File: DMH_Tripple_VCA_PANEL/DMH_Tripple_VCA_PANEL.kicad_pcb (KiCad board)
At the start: 2 copper layers, 50 x 200 mm, 21 parts, among them J0 Panel_GND_Solder_Wire_Pad

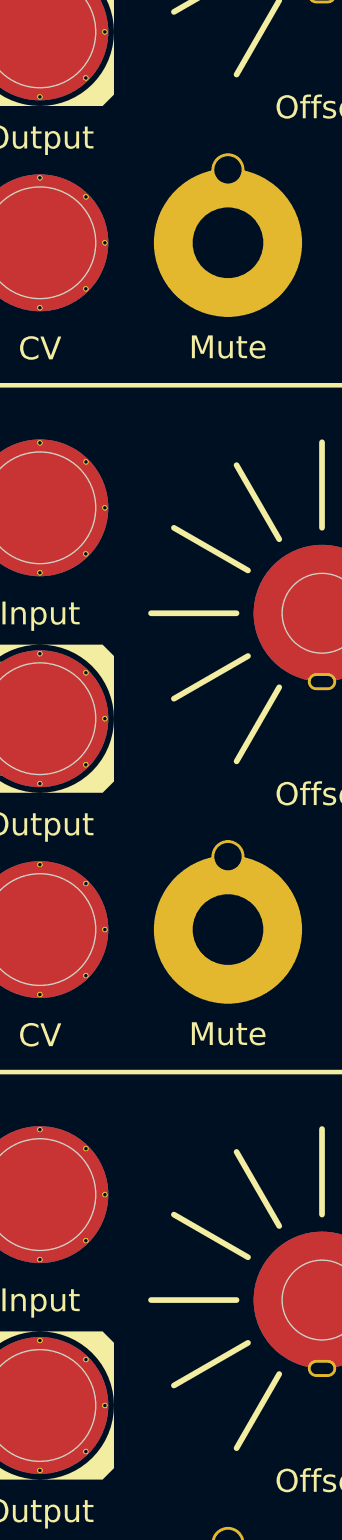
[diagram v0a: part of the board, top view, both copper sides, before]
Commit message: Added LED holes
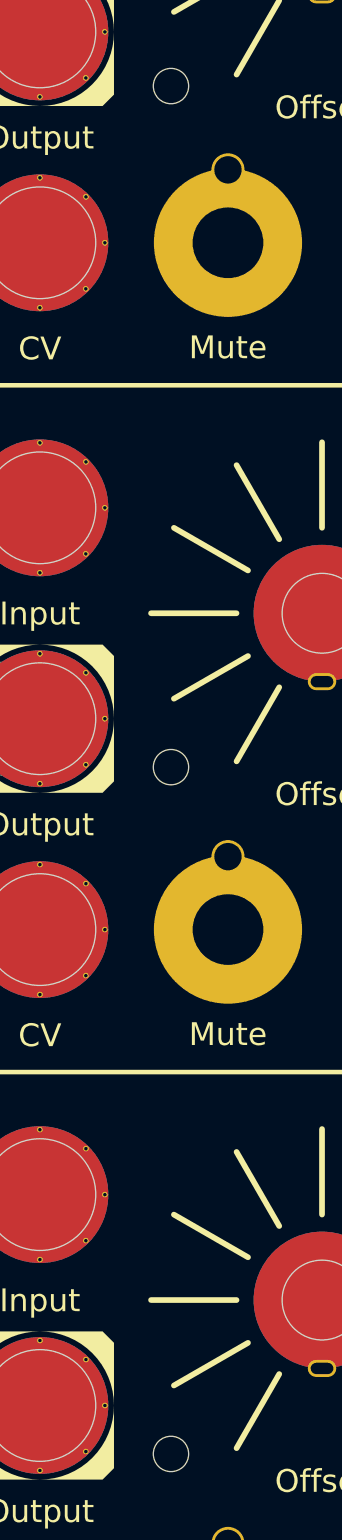
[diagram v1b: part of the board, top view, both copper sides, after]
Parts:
- added H17: LED, SynthStuff:MountingHole_LED_3mm, F.Cu at (70.0, 74.5)
- added H22: LED, SynthStuff:MountingHole_LED_3mm, F.Cu at (70.0, 134.2)
- added H23: LED, SynthStuff:MountingHole_LED_3mm, F.Cu at (70.0, 194.5)

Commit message: Finished Schematic
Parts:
- H17, H22, H23: footprint SynthStuff:MountingHole_LED_3mm -> SynthStuff:MountingHole_LED_5mm
- H18: value Mix Out + -> Mix Out
- moved J0 40.0 mm to (95.0, 130.0)

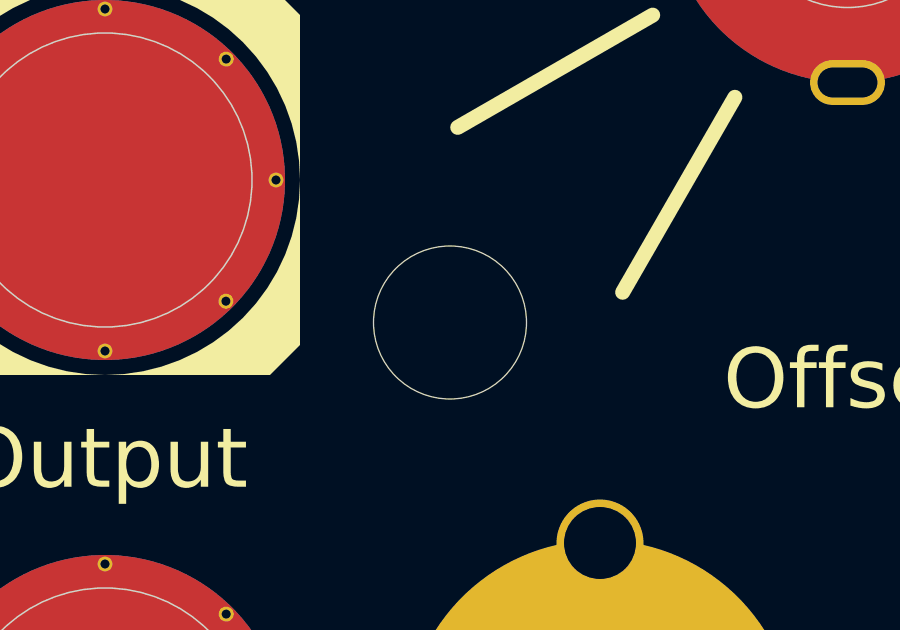
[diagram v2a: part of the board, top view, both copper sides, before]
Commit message: Fixed LED position
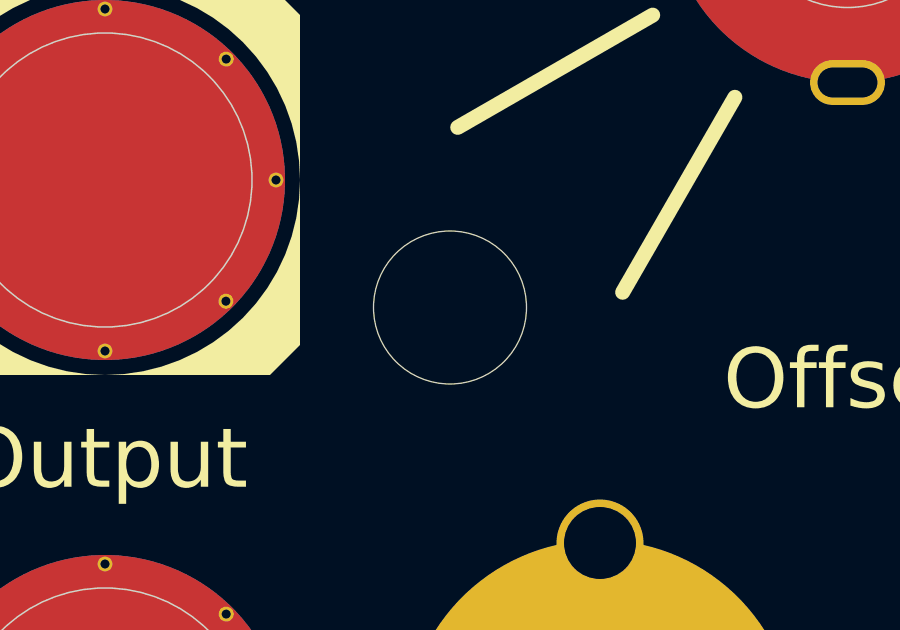
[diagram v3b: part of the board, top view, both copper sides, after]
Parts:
- moved H17 0.50 mm to (70.0, 74.0)
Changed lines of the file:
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@@
 	(footprint "SynthStuff:MountingHole_LED_5mm"
 		(layer "F.Cu")
-		(at 70 74.5)
+		(at 70 74)
 		(descr "Mounting Hole 3mm, no annular")
 		(tags "mounting hole 3mm no annular")

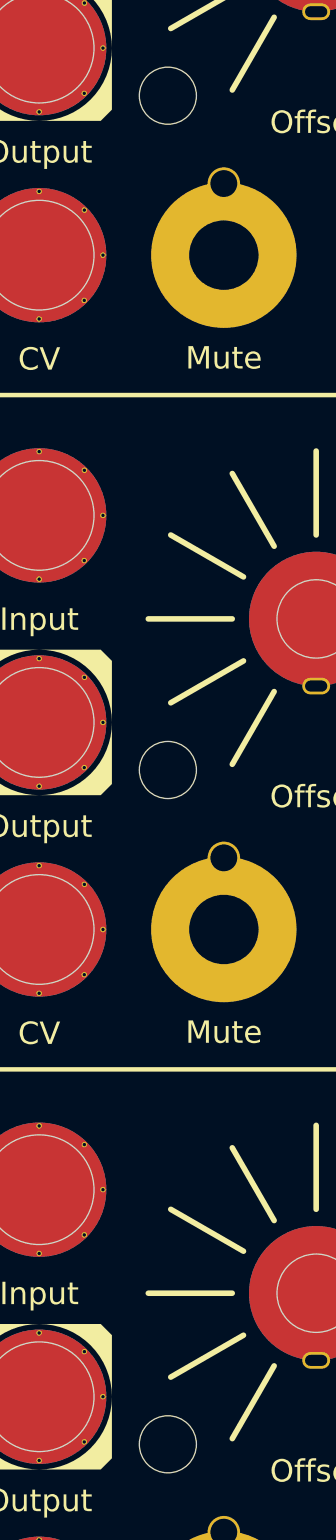
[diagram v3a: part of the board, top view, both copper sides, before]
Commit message: Changed LEDs to bi-color
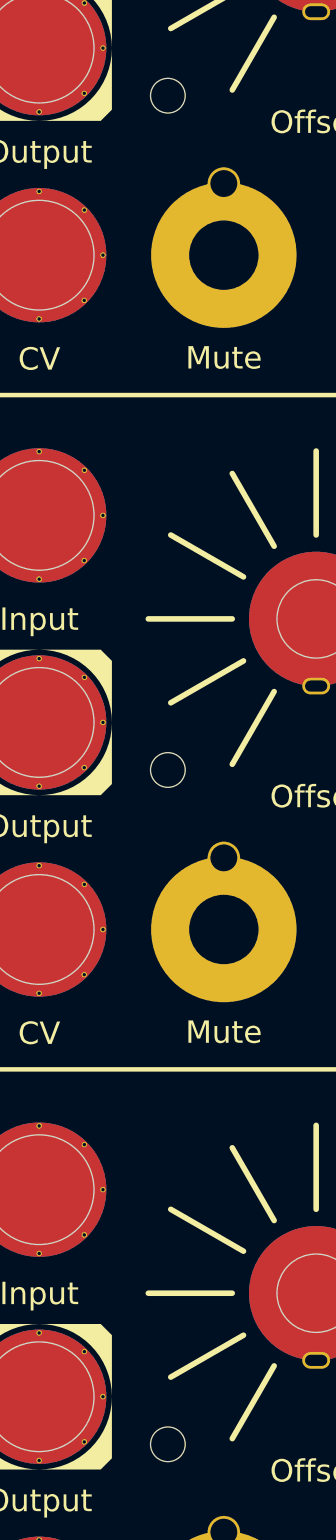
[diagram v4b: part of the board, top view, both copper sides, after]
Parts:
- H17, H22, H23: footprint SynthStuff:MountingHole_LED_5mm -> SynthStuff:MountingHole_LED_3mm
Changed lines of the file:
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@@
 		)
 	)
-	(footprint "SynthStuff:MountingHole_LED_5mm"
+	(footprint "SynthStuff:MountingHole_LED_3mm"
 		(layer "F.Cu")
 		(at 70 134.25)
@@
 			)
 		)
-		(property "Footprint" "SynthStuff:MountingHole_LED_5mm"
+		(property "Footprint" "SynthStuff:MountingHole_LED_3mm"
 			(at 0 0 0)
 			(unlocked yes)
@@
 		(fp_circle
 			(center 0 0)
-			(end 3 0)
+			(end 2 0)
 			(stroke
 				(width 0.15)
@@
 		(fp_circle
 			(center 0 0)
-			(end 3.25 0)
+			(end 2.25 0)
 			(stroke
 				(width 0.05)
@@
 		(pad "" np_thru_hole circle
 			(at 0 0)
-			(size 5.1 5.1)
-			(drill 5.1)
+			(size 3.1 3.1)
+			(drill 3.1)
 			(layers "F&B.Cu" "*.Mask")
 		)
-		(model "${KICAD8_3DMODEL_DIR}/LED_THT.3dshapes/LED_D5.0mm.step"
+		(model "${KICAD8_3DMODEL_DIR}/LED_THT.3dshapes/LED_D3.0mm.step"
 			(offset
 				(xyz -1.3 0 -6.5)
@@
 		)
 	)
-	(footprint "SynthStuff:MountingHole_LED_5mm"
+	(footprint "SynthStuff:MountingHole_LED_3mm"
 		(layer "F.Cu")
 		(at 70 194.5)
@@
 			)
 		)
-		(property "Footprint" "SynthStuff:MountingHole_LED_5mm"
+		(property "Footprint" "SynthStuff:MountingHole_LED_3mm"
 			(at 0 0 0)
 			(unlocked yes)
@@
 		(fp_circle
 			(center 0 0)
-			(end 3 0)
+			(end 2 0)
 			(stroke
 				(width 0.15)
@@
 		(fp_circle
 			(center 0 0)
-			(end 3.25 0)
+			(end 2.25 0)
 			(stroke
 				(width 0.05)
@@
 		(pad "" np_thru_hole circle
 			(at 0 0)
-			(size 5.1 5.1)
-			(drill 5.1)
+			(size 3.1 3.1)
+			(drill 3.1)
 			(layers "F&B.Cu" "*.Mask")
 		)
-		(model "${KICAD8_3DMODEL_DIR}/LED_THT.3dshapes/LED_D5.0mm.step"
+		(model "${KICAD8_3DMODEL_DIR}/LED_THT.3dshapes/LED_D3.0mm.step"
 			(offset
 				(xyz -1.3 0 -6.5)
@@
 		)
 	)
-	(footprint "SynthStuff:MountingHole_LED_5mm"
+	(footprint "SynthStuff:MountingHole_LED_3mm"
 		(layer "F.Cu")
 		(at 70 74)
@@
 			)
 		)
-		(property "Footprint" "SynthStuff:MountingHole_LED_5mm"
+		(property "Footprint" "SynthStuff:MountingHole_LED_3mm"
 			(at 0 0 0)
 			(unlocked yes)
@@
 		(fp_circle
 			(center 0 0)
-			(end 3 0)
+			(end 2 0)
 			(stroke
 				(width 0.15)
@@
 		(fp_circle
 			(center 0 0)
-			(end 3.25 0)
+			(end 2.25 0)
 			(stroke
 				(width 0.05)
@@
 		(pad "" np_thru_hole circle
 			(at 0 0)
-			(size 5.1 5.1)
-			(drill 5.1)
+			(size 3.1 3.1)
+			(drill 3.1)
 			(layers "F&B.Cu" "*.Mask")
 		)
-		(model "${KICAD8_3DMODEL_DIR}/LED_THT.3dshapes/LED_D5.0mm.step"
+		(model "${KICAD8_3DMODEL_DIR}/LED_THT.3dshapes/LED_D3.0mm.step"
 			(offset
 				(xyz -1.3 0 -6.5)

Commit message: Generated Gerbers
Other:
- board text added: "074-3"
- board text added: "Mk1.0 - March 2025"
- board text removed: "BJT-3"
- board text removed: "Mk1.0 - Month Year"
